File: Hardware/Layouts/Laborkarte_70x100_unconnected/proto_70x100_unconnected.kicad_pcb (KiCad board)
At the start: 2 copper layers, 70 x 100 mm, 722 parts

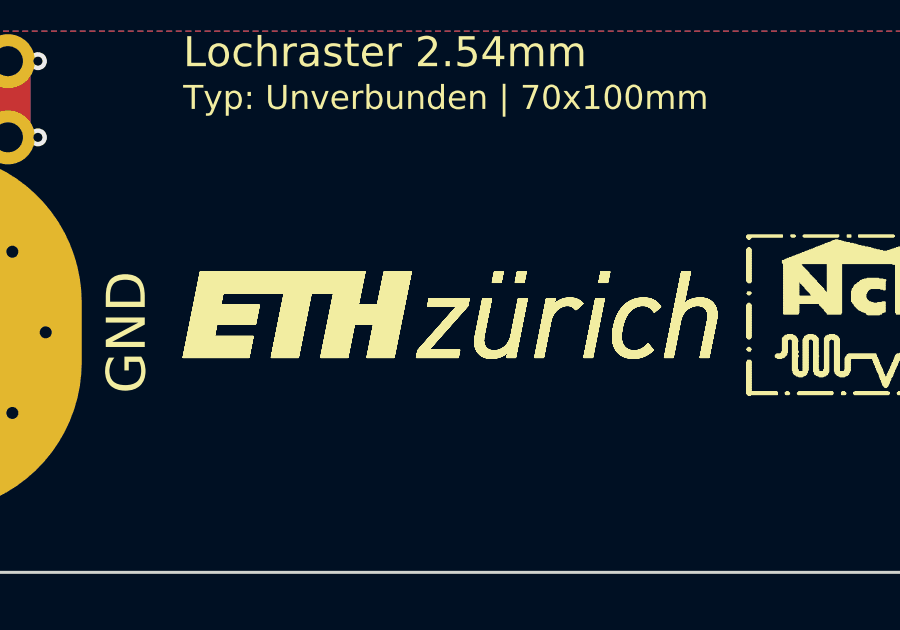
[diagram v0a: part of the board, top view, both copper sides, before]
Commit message: Fix ETH logo visibility, add violet PCB background, show F+B sides
- Downscale high-res logo images before rasterizing so line width
  stays visible (ETH logo was 0.005mm, now 0.02mm)
- Preview images now show front and back side by side
- Board background changed to JLCPCB violet
- PDF updated with filled copper zones and fixed silkscreen parsing
- All Gerbers and ZIPs regenerated
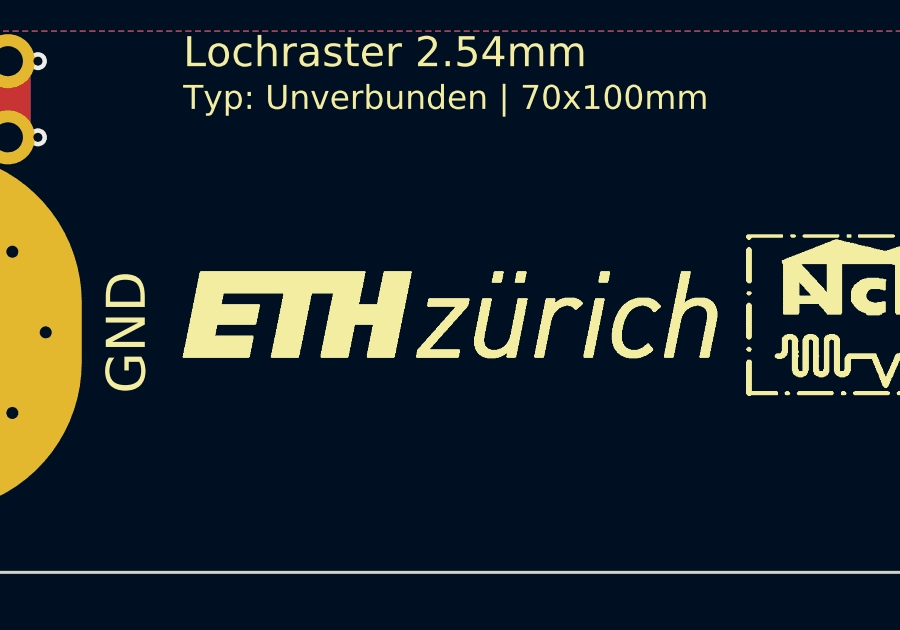
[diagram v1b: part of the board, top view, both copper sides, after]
